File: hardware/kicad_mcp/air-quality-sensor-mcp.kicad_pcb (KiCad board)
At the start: 2 copper layers, 80 x 60 mm, 16 parts, among them J1 JST_PH_2pin_Battery, U1 XIAO_ESP32C3, U2 Adafruit_SCD41, U3 Adafruit_SGP41, U4 SSD1306_OLED_128x64, U5 TP4056_USB-C_Module

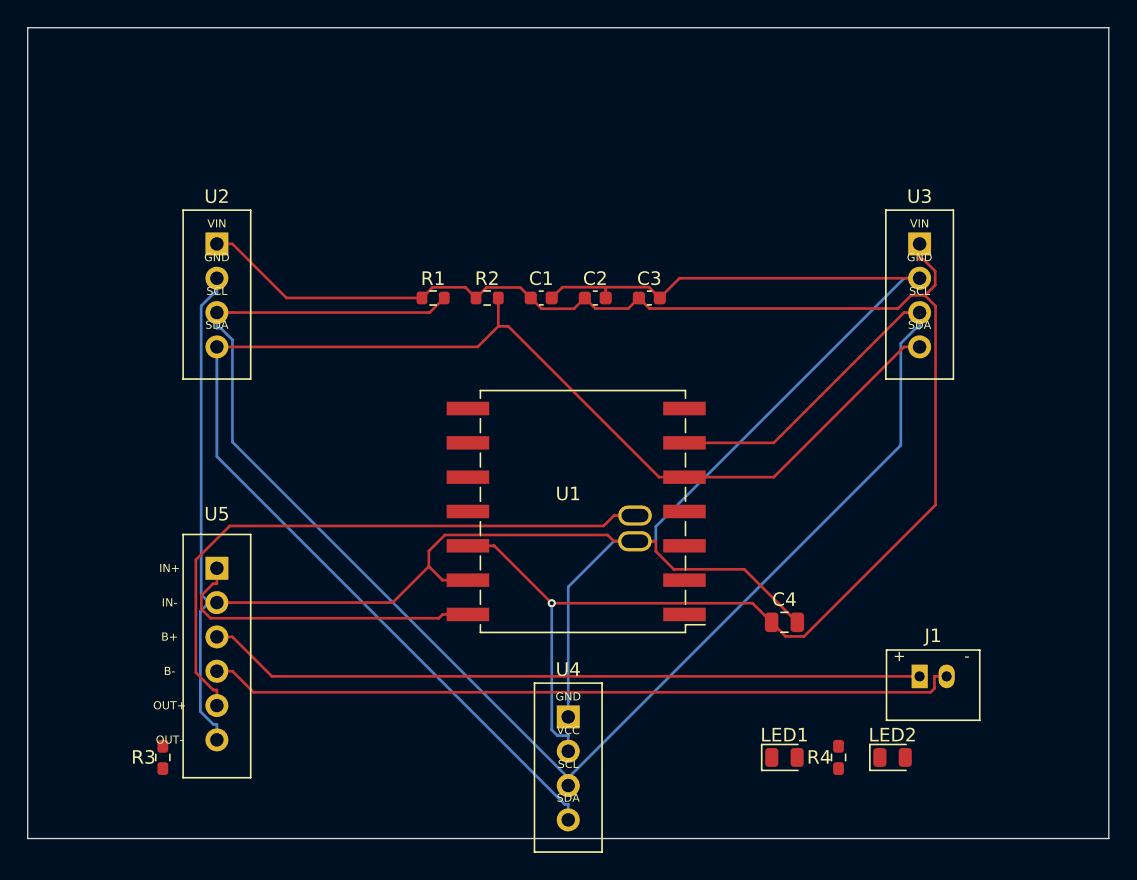
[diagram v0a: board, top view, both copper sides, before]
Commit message: Finalize v3 MCP board respin: PMSA003I PM sensor + 5 V boost power tree
Commit the June 2026 design session that was never landed: U1 switched to a
through-hole DIP footprint, Adafruit PMSA003I (U6) added on the shared I2C
bus, TPS61023-class 5 V boost (U7) + SS14 Schottky (D1) power tree for
battery-only operation. 19 symbols, ERC 0 errors, 160 routed tracks, DRC
clean; manufacturing outputs regenerated. BOARD-DESIGN-NOTES.md records
board-specific status and open items; MCP-FUTURE-CHANGES.md records the
MCP-only workflow policy and validation baseline. Ignore local KiCad/MCP
editor artifacts (prl, validation caches, eval scratch files).
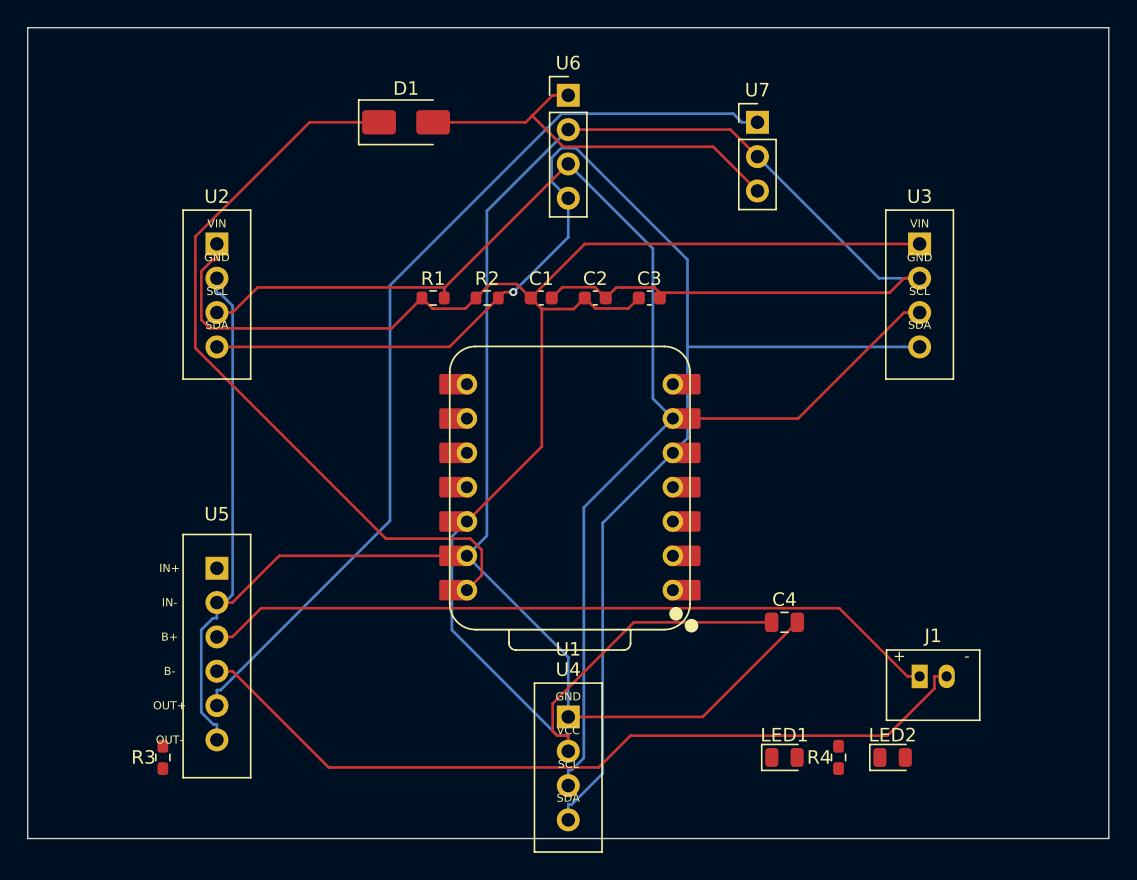
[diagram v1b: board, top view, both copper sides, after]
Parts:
- added D1: D_SMA, D_SMA, F.Cu at (38.0, 17.0)
- added U6: PinHeader_1x04_P2.54mm_Vertical, PinHeader_1x04_P2.54mm_Vertical, F.Cu at (50.0, 15.0)
- added U7: PinHeader_1x03_P2.54mm_Vertical, PinHeader_1x03_P2.54mm_Vertical, F.Cu at (64.0, 17.0)
- U1: footprint AirQuality:XIAO_ESP32C3 -> Seeed_XIAO:XIAO-ESP32C3-DIP
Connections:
- U1 pad 14: USB_5V -> XIAO_5V
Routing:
- net XIAO_5V: track 0.00 -> 57.0 mm
- net +5V: track 0.00 -> 29.8 mm
- net I2C_SCL: track 130.0 -> 105.4 mm
- net VBAT: track 45.4 -> 69.3 mm
- net USB_5V: track 23.8 -> 0.00 mm
- net GND: track 163.7 -> 186.4 mm
- net +3V3: track 131.3 -> 136.6 mm, vias 1 -> 0
- net BAT-: track 55.7 -> 60.3 mm
- net I2C_SDA: track 109.3 -> 112.8 mm, vias 0 -> 1
- net BAT+: track 53.2 -> 55.0 mm
- net Net-(U1-9): track 0.00 -> 0.84 mm
- net Net-(U1-8): track 0.00 -> 0.84 mm
- net Net-(U1-7): track 0.00 -> 0.84 mm
- net Net-(U1-4): track 0.00 -> 0.84 mm
- net Net-(U1-3): track 0.00 -> 0.84 mm
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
